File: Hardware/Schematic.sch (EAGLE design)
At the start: 27 parts, among them IC1 XC6220A331MR-G, J1 SAMACSYS_PARTS_USB4110-GF-A, J4 112A-TAAR-R03_ATTEND, Q1 20V/4.2A/52mΩ/1.4W, Q2 SI1308EDL-T1-GE3

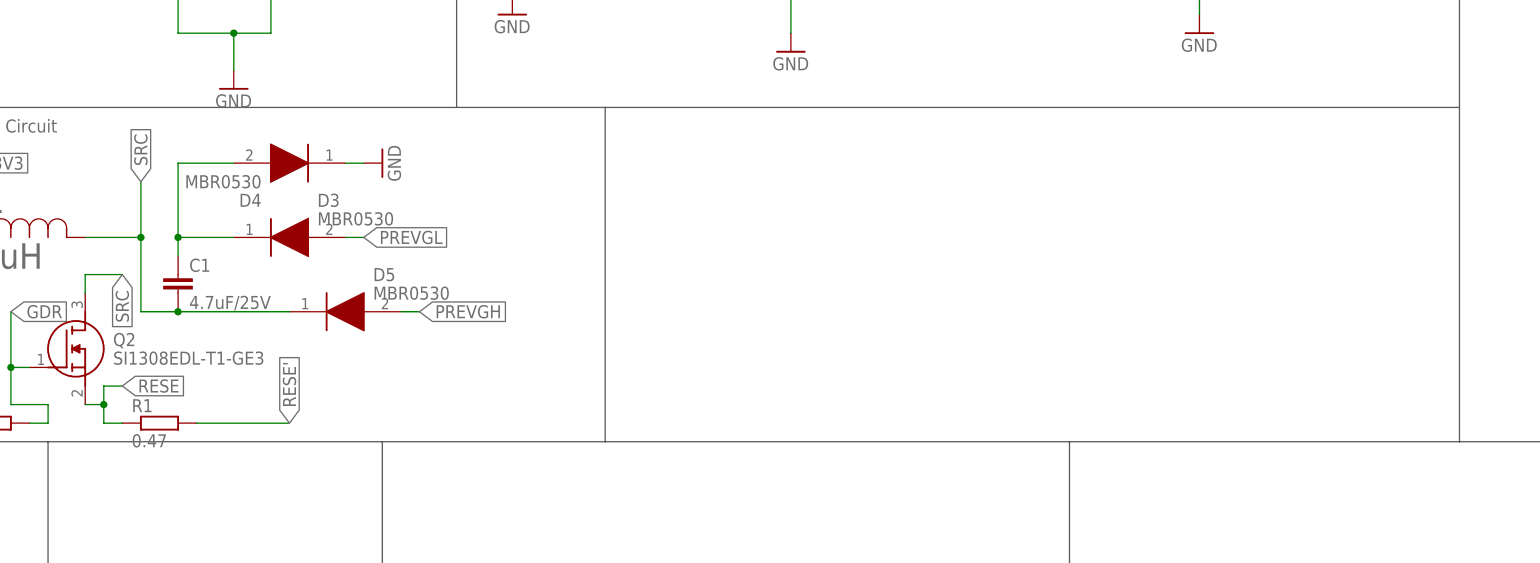
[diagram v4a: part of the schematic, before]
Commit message: add  Li-Po Battery Charging Controller
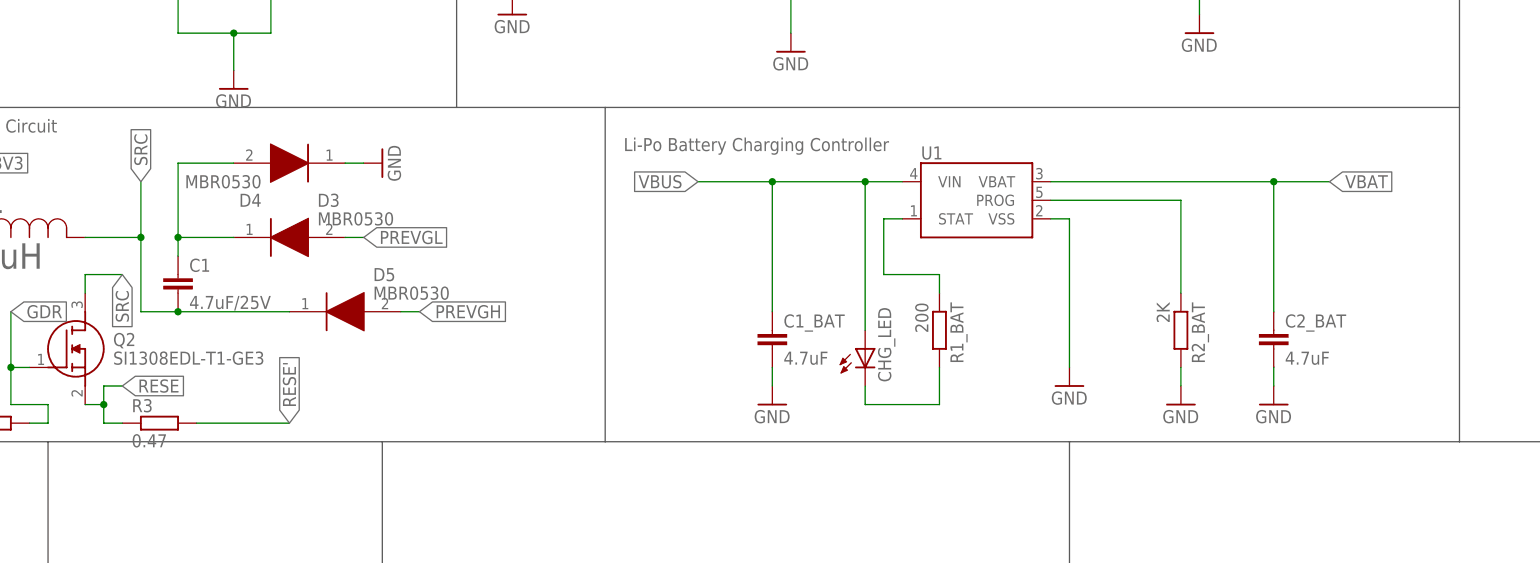
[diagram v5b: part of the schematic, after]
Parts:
- added C1_BAT, C2_BAT: 4.7uF, DeskAssistant v19 v1.flbr:EAGLE-LTSPICE_CC0402
- added CHG_LED: (no value), DeskAssistant v19 v1.flbr:ADAFRUIT_LEDCHIP-LED0603
- added R1_BAT: 200, DeskAssistant v19 v1.flbr:ESP32_WROVER_EAGLE-LTSPICE_RR0402
- added R2_BAT: 2K, DeskAssistant v19 v1.flbr:ESP32_WROVER_EAGLE-LTSPICE_RR0402
- added U1: ESP32_WROVER_SPARKFUN-IC-POWER_MCP73831, DeskAssistant v19 v1.flbr:ESP32_WROVER_SPARKFUN-IC-POWER_MCP73831
- renumbered R1 to R3
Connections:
- new net N$5: R2_BAT.1, U1.PROG
- new net N$7: R1_BAT.1, U1.STAT
- new net N$8: CHG_LED.C, R1_BAT.2
- net GND: now also C1_BAT.2, C2_BAT.2, R2_BAT.2, U1.VSS
- net VBAT: now also C2_BAT.1, U1.VBAT
- net VBUS: now also C1_BAT.1, CHG_LED.A, U1.VIN
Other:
- note added: "Li-Po Battery Charging Controller"
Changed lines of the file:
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@@
 <part name="GND16" library="DeskAssistant v19 v1.flbr" library_urn="urn:adsk.wipprod:fs.file:vf.vVvdDOfaSfavM5thX5SjWw" deviceset="GND" device=""/>
 <part name="Q2" library="DeskAssistant v19 v1.flbr" library_urn="urn:adsk.wipprod:fs.file:vf.vVvdDOfaSfavM5thX5SjWw" deviceset="SI1308EDL-T1-GE3" device=""/>
-<part name="R1" library="DeskAssistant v19 v1.flbr" library_urn="urn:adsk.wipprod:fs.file:vf.vVvdDOfaSfavM5thX5SjWw" deviceset="ESP32_WROVER_EAGLE-LTSPICE_R" device="R0402" value="0.47"/>
+<part name="R3" library="DeskAssistant v19 v1.flbr" library_urn="urn:adsk.wipprod:fs.file:vf.vVvdDOfaSfavM5thX5SjWw" deviceset="ESP32_WROVER_EAGLE-LTSPICE_R" device="R0402" value="0.47"/>
 <part name="R4" library="DeskAssistant v19 v1.flbr" library_urn="urn:adsk.wipprod:fs.file:vf.vVvdDOfaSfavM5thX5SjWw" deviceset="ESP32_WROVER_EAGLE-LTSPICE_R" device="R0402" value="10K"/>
 <part name="GND17" library="DeskAssistant v19 v1.flbr" library_urn="urn:adsk.wipprod:fs.file:vf.vVvdDOfaSfavM5thX5SjWw" deviceset="GND" device=""/>
+<part name="U1" library="DeskAssistant v19 v1.flbr" library_urn="urn:adsk.wipprod:fs.file:vf.vVvdDOfaSfavM5thX5SjWw" deviceset="ESP32_WROVER_SPARKFUN-IC-POWER_MCP73831" device=""/>
+<part name="C2_BAT" library="DeskAssistant v19 v1.flbr" library_urn="urn:adsk.wipprod:fs.file:vf.vVvdDOfaSfavM5thX5SjWw" deviceset="EAGLE-LTSPICE_C" device="C0402" value="4.7uF"/>
+<part name="C1_BAT" library="DeskAssistant v19 v1.flbr" library_urn="urn:adsk.wipprod:fs.file:vf.vVvdDOfaSfavM5thX5SjWw" deviceset="EAGLE-LTSPICE_C" device="C0402" value="4.7uF"/>
+<part name="GND18" library="DeskAssistant v19 v1.flbr" library_urn="urn:adsk.wipprod:fs.file:vf.vVvdDOfaSfavM5thX5SjWw" deviceset="GND" device=""/>
+<part name="GND19" library="DeskAssistant v19 v1.flbr" library_urn="urn:adsk.wipprod:fs.file:vf.vVvdDOfaSfavM5thX5SjWw" deviceset="GND" device=""/>
+<part name="GND20" library="DeskAssistant v19 v1.flbr" library_urn="urn:adsk.wipprod:fs.file:vf.vVvdDOfaSfavM5thX5SjWw" deviceset="GND" device=""/>
+<part name="R1_BAT" library="DeskAssistant v19 v1.flbr" library_urn="urn:adsk.wipprod:fs.file:vf.vVvdDOfaSfavM5thX5SjWw" deviceset="ESP32_WROVER_EAGLE-LTSPICE_R" device="R0402" value="200"/>
+<part name="R2_BAT" library="DeskAssistant v19 v1.flbr" library_urn="urn:adsk.wipprod:fs.file:vf.vVvdDOfaSfavM5thX5SjWw" deviceset="ESP32_WROVER_EAGLE-LTSPICE_R" device="R0402" value="2K"/>
+<part name="GND21" library="DeskAssistant v19 v1.flbr" library_urn="urn:adsk.wipprod:fs.file:vf.vVvdDOfaSfavM5thX5SjWw" deviceset="GND" device=""/>
+<part name="CHG_LED" library="DeskAssistant v19 v1.flbr" library_urn="urn:adsk.wipprod:fs.file:vf.vVvdDOfaSfavM5thX5SjWw" deviceset="ADAFRUIT_LED" device="CHIP-LED0603"/>
 </parts>
 <sheets>
@@
 <text x="-147.32" y="210.82" size="1.778" layer="95" align="center">Display Type Selector</text>
 <text x="-86.36" y="210.82" size="1.778" layer="95" align="center">E-Paper Drive Circuit</text>
+<text x="20.32" y="208.28" size="1.778" layer="95" align="center"> Li-Po Battery Charging Controller
+</text>
 </plain>
 <instances>
@@
 <attribute name="VALUE" x="-67.31" y="179.07" size="1.778" layer="96" align="center-left"/>
 </instance>
-<instance part="R1" gate="G$1" x="-60.96" y="170.18" smashed="yes">
+<instance part="R3" gate="G$1" x="-60.96" y="170.18" smashed="yes">
 <attribute name="NAME" x="-64.77" y="171.6786" size="1.778" layer="95"/>
 <attribute name="VALUE" x="-64.77" y="166.878" size="1.778" layer="96"/>
@@
 <instance part="GND17" gate="1" x="-93.98" y="170.18" smashed="yes" rot="R270">
 <attribute name="VALUE" x="-96.52" y="172.72" size="1.778" layer="96" rot="R270"/>
+</instance>
+<instance part="U1" gate="G$1" x="50.8" y="200.66" smashed="yes">
+<attribute name="NAME" x="43.18" y="206.248" size="1.778" layer="95"/>
+</instance>
+<instance part="C2_BAT" gate="G$1" x="91.44" y="182.88" smashed="yes">
+<attribute name="NAME" x="92.964" y="183.261" size="1.778" layer="95"/>
+<attribute name="VALUE" x="92.964" y="178.181" size="1.778" layer="96"/>
+</instance>
+<instance part="C1_BAT" gate="G$1" x="22.86" y="182.88" smashed="yes">
+<attribute name="NAME" x="24.384" y="183.261" size="1.778" layer="95"/>
+<attribute name="VALUE" x="24.384" y="178.181" size="1.778" layer="96"/>
+</instance>
+<instance part="GND18" gate="1" x="91.44" y="172.72" smashed="yes">
+<attribute name="VALUE" x="88.9" y="170.18" size="1.778" layer="96"/>
+</instance>
+<instance part="GND19" gate="1" x="22.86" y="172.72" smashed="yes">
+<attribute name="VALUE" x="20.32" y="170.18" size="1.778" layer="96"/>
+</instance>
+<instance part="GND20" gate="1" x="63.5" y="175.26" smashed="yes">
+<attribute name="VALUE" x="60.96" y="172.72" size="1.778" layer="96"/>
+</instance>
+<instance part="R1_BAT" gate="G$1" x="45.72" y="182.88" smashed="yes" rot="R270">
+<attribute name="NAME" x="47.2186" y="186.69" size="1.778" layer="95" rot="R270"/>
+<attribute name="VALUE" x="42.418" y="186.69" size="1.778" layer="96" rot="R270"/>
+<attribute name="NAME" x="47.2186" y="186.69" size="1.778" layer="95" rot="R270"/>
+<attribute name="VALUE" x="42.418" y="186.69" size="1.778" layer="96" rot="R270"/>
+</instance>
+<instance part="R2_BAT" gate="G$1" x="78.74" y="182.88" smashed="yes" rot="R270">
+<attribute name="NAME" x="80.2386" y="186.69" size="1.778" layer="95" rot="R270"/>
+<attribute name="VALUE" x="75.438" y="186.69" size="1.778" layer="96" rot="R270"/>
+<attribute name="NAME" x="80.2386" y="186.69" size="1.778" layer="95" rot="R270"/>
+<attribute name="VALUE" x="75.438" y="186.69" size="1.778" layer="96" rot="R270"/>
+</instance>
+<instance part="GND21" gate="1" x="78.74" y="172.72" smashed="yes">
+<attribute name="VALUE" x="76.2" y="170.18" size="1.778" layer="96"/>
+</instance>
+<instance part="CHG_LED" gate="G$1" x="35.56" y="180.34" smashed="yes">
+<attribute name="NAME" x="39.116" y="175.768" size="1.778" layer="95" rot="R90"/>
+<attribute name="VALUE" x="41.275" y="175.768" size="1.778" layer="96" rot="R90"/>
 </instance>
 </instances>
@@
 <pinref part="GND17" gate="1" pin="GND"/>
 </segment>
+<segment>
+<pinref part="C2_BAT" gate="G$1" pin="2"/>
+<wire x1="91.44" y1="177.8" x2="91.44" y2="175.26" width="0.1524" layer="91"/>
+<pinref part="GND18" gate="1" pin="GND"/>
+</segment>
+<segment>
+<pinref part="C1_BAT" gate="G$1" pin="2"/>
+<wire x1="22.86" y1="177.8" x2="22.86" y2="175.26" width="0.1524" layer="91"/>
+<pinref part="GND19" gate="1" pin="GND"/>
+</segment>
+<segment>
+<pinref part="U1" gate="G$1" pin="VSS"/>
+<wire x1="60.96" y1="198.12" x2="63.5" y2="198.12" width="0.1524" layer="91"/>
+<wire x1="63.5" y1="198.12" x2="63.5" y2="177.8" width="0.1524" layer="91"/>
+<pinref part="GND20" gate="1" pin="GND"/>
+</segment>
+<segment>
+<pinref part="R2_BAT" gate="G$1" pin="2"/>
+<wire x1="78.74" y1="177.8" x2="78.74" y2="175.26" width="0.1524" layer="91"/>
+<pinref part="GND21" gate="1" pin="GND"/>
+</segment>
 </net>
 <net name="VUSB" class="0">
@@
 <junction x="-12.7" y="259.08"/>
 <pinref part="R1_PWRUSB" gate="G$1" pin="2"/>
+</segment>
+<segment>
+<pinref part="C1_BAT" gate="G$1" pin="1"/>
+<wire x1="22.86" y1="185.42" x2="22.86" y2="203.2" width="0.1524" layer="91"/>
+<wire x1="22.86" y1="203.2" x2="35.56" y2="203.2" width="0.1524" layer="91"/>
+<pinref part="U1" gate="G$1" pin="VIN"/>
+<wire x1="35.56" y1="203.2" x2="40.64" y2="203.2" width="0.1524" layer="91"/>
+<wire x1="22.86" y1="203.2" x2="12.7" y2="203.2" width="0.1524" layer="91"/>
+<junction x="22.86" y="203.2"/>
+<label x="12.7" y="203.2" size="1.778" layer="95" rot="R180" xref="yes"/>
+<pinref part="CHG_LED" gate="G$1" pin="A"/>
+<wire x1="35.56" y1="182.88" x2="35.56" y2="203.2" width="0.1524" layer="91"/>
+<junction x="35.56" y="203.2"/>
 </segment>
 </net>
@@
 <label x="20.32" y="269.24" size="1.778" layer="95" xref="yes"/>
 </segment>
+<segment>
+<pinref part="U1" gate="G$1" pin="VBAT"/>
+<wire x1="60.96" y1="203.2" x2="91.44" y2="203.2" width="0.1524" layer="91"/>
+<label x="99.06" y="203.2" size="1.778" layer="95" xref="yes"/>
+<pinref part="C2_BAT" gate="G$1" pin="1"/>
+<wire x1="91.44" y1="203.2" x2="99.06" y2="203.2" width="0.1524" layer="91"/>
+<wire x1="91.44" y1="185.42" x2="91.44" y2="203.2" width="0.1524" layer="91"/>
+<junction x="91.44" y="203.2"/>
+</segment>
 </net>
 <net name="SS_SD" class="0">
@@
 </segment>
 <segment>
-<pinref part="R1" gate="G$1" pin="2"/>
+<pinref part="R3" gate="G$1" pin="2"/>
 <wire x1="-55.88" y1="170.18" x2="-43.18" y2="170.18" width="0.1524" layer="91"/>
 <label x="-43.18" y="170.18" size="1.778" layer="95" rot="R90" xref="yes"/>
@@
 <junction x="-68.58" y="172.72"/>
 <wire x1="-68.58" y1="170.18" x2="-66.04" y2="170.18" width="0.1524" layer="91"/>
-<pinref part="R1" gate="G$1" pin="1"/>
-</segment>
-</net>
+<pinref part="R3" gate="G$1" pin="1"/>
+</segment>
+</net>
+<net name="N$5" class="0">
+<segment>
+<pinref part="U1" gate="G$1" pin="PROG"/>
+<wire x1="60.96" y1="200.66" x2="78.74" y2="200.66" width="0.1524" layer="91"/>
+<wire x1="78.74" y1="200.66" x2="78.74" y2="187.96" width="0.1524" layer="91"/>
+<pinref part="R2_BAT" gate="G$1" pin="1"/>
+</segment>
+</net>
+<net name="N$7" class="0">
+<segment>
+<pinref part="U1" gate="G$1" pin="STAT"/>
+<wire x1="40.64" y1="198.12" x2="38.1" y2="198.12" width="0.1524" layer="91"/>
+<wire x1="38.1" y1="198.12" x2="38.1" y2="190.5" width="0.1524" layer="91"/>
+<wire x1="38.1" y1="190.5" x2="45.72" y2="190.5" width="0.1524" layer="91"/>
+<wire x1="45.72" y1="190.5" x2="45.72" y2="187.96" width="0.1524" layer="91"/>
+<pinref part="R1_BAT" gate="G$1" pin="1"/>
+</segment>
+</net>
+<net name="N$8" class="0">
+<segment>
+<pinref part="R1_BAT" gate="G$1" pin="2"/>
+<wire x1="45.72" y1="177.8" x2="45.72" y2="172.72" width="0.1524" layer="91"/>
+<wire x1="45.72" y1="172.72" x2="35.56" y2="172.72" width="0.1524" layer="91"/>
+<wire x1="35.56" y1="172.72" x2="35.56" y2="175.26" width="0.1524" layer="91"/>
+<pinref part="CHG_LED" gate="G$1" pin="C"/>
+</segment>
+</net>

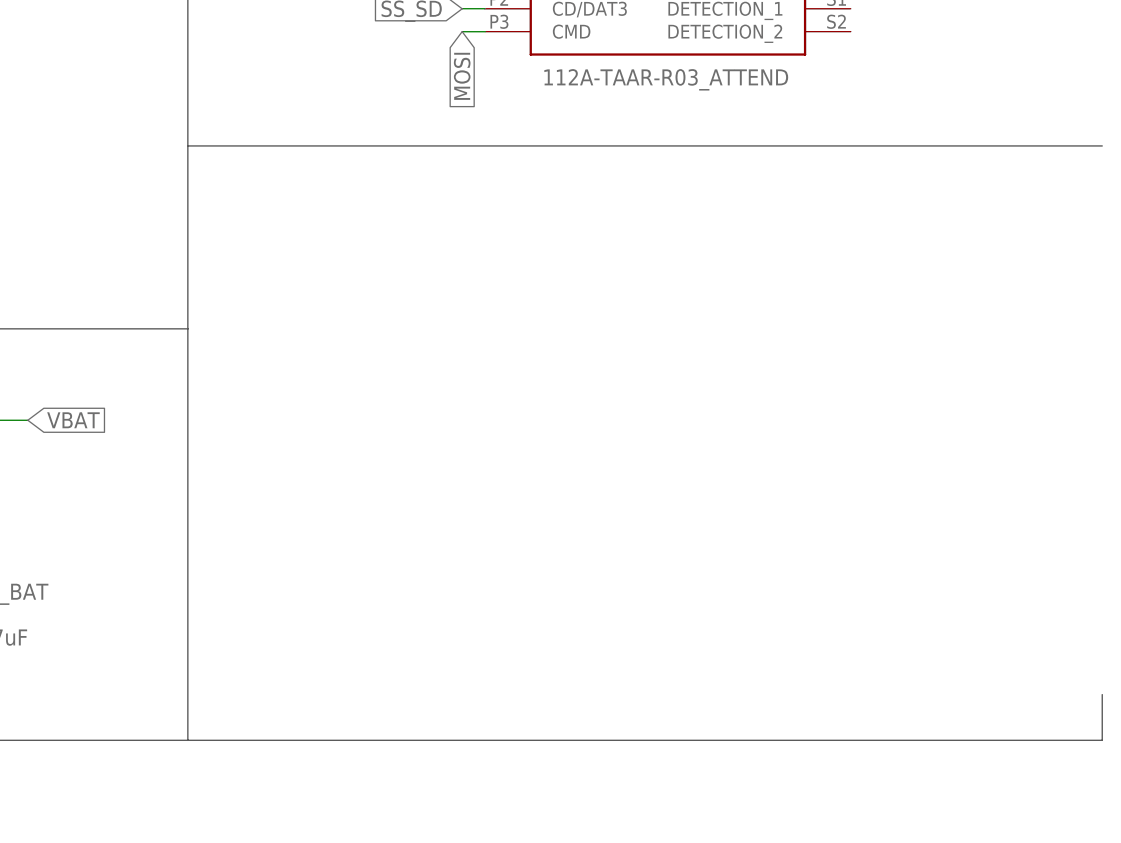
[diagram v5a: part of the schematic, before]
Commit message: add ESP32 C6 + vscode settings
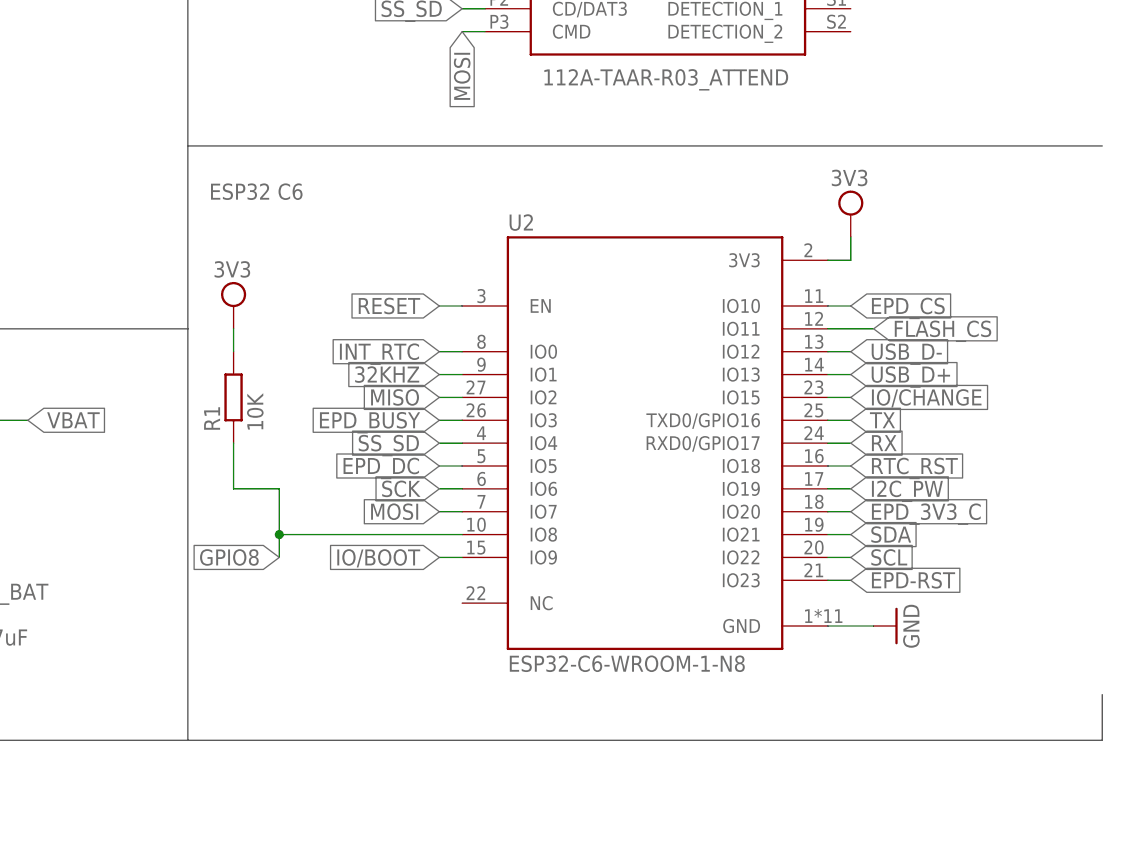
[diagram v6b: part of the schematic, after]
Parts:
- added R1: 10K, DeskAssistant v19 v1.flbr:ESP32_WROVER_EAGLE-LTSPICE_RR0402
- added U2: ESP32-C6-WROOM-1-N8, DeskAssistant v19 v1.flbr:ESP32-C6-WROOM-1-N8
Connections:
- new net 32KHZ: U2.IO1
- new net EPD-RST: U2.IO23
- new net EPD_3V3_C: U2.IO20
- new net EPD_BUSY: U2.IO3
- new net EPD_CS: U2.IO10
- new net EPD_DC: U2.IO5
- new net FLASH_CS: U2.IO11
- new net GPIO8: R1.1, U2.IO8
- new net I2C_PW: U2.IO19
- new net INT_RTC: U2.IO0
- new net IO/BOOT: U2.IO9
- new net IO/CHANGE: U2.IO15
- new net RESET: U2.EN
- new net RTC_RST: U2.IO18
- new net RX: U2.RXD0/GPIO17
- new net SCL: U2.IO22
- new net SDA: U2.IO21
- new net TX: U2.TXD0/GPIO16
- net 3V3: now also R1.2, U2.3V3
- net GND: now also U2.GND
- net MISO: now also U2.IO2
- net MOSI: now also U2.IO7
- net SCK: now also U2.IO6
- net SS_SD: now also U2.IO4
- net USB_D+: now also U2.IO13
- net USB_D-: now also U2.IO12
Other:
- note added: "ESP32 C6"

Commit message: add E-Paper Display Header
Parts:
- added EPD_C1, EPD_C10, EPD_C11, EPD_C12, EPD_C2, EPD_C6, EPD_C7, EPD_C8, EPD_C9: 1uF/50V, DeskAssistant v19 v1.flbr:EAGLE-LTSPICE_CC0402
- added EPD_C5: 0.1uF/50V, DeskAssistant v19 v1.flbr:EAGLE-LTSPICE_CC0402
- added J2: FH34SRJ-24S-0.5SH_99_, DeskAssistant v19 v1.flbr:FH34SRJ-24S-0.5SH_99_
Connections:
- new net EPD_RST: J2.10
- new net N$10: EPD_C2.2, J2.5
- new net N$11: EPD_C5.2, J2.15
- new net N$12: EPD_C12.2, J2.24
- new net N$13: EPD_C11.2, J2.23
- new net N$14: EPD_C10.2, J2.22
- new net N$16: EPD_C8.2, J2.20
- new net N$17: EPD_C7.2, J2.19
- new net N$18: EPD_C6.2, J2.18
- new net N$9: EPD_C1.2, J2.4
- net EPD_3V3: now also J2.16, J2.17
- net EPD_BUSY: now also J2.9
- net EPD_CS: now also J2.12
- net EPD_DC: now also J2.11
- net GDR: now also J2.2
- net GND: now also EPD_C1.1, J2.8, J2.MP1, J2.MP2
- net MOSI: now also J2.14
- net PREVGH: now also EPD_C9.2, J2.21
- net PREVGL: now also EPD_C10.1, EPD_C11.1, EPD_C12.1, EPD_C5.1, EPD_C6.1, EPD_C7.1, EPD_C8.1, EPD_C9.1
- net RESE: now also J2.3
- net SCK: now also J2.13
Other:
- note added: "E-Paper Display Header"
